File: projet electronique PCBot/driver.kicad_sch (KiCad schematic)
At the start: 1 part, among them U4 DRV8833PWP

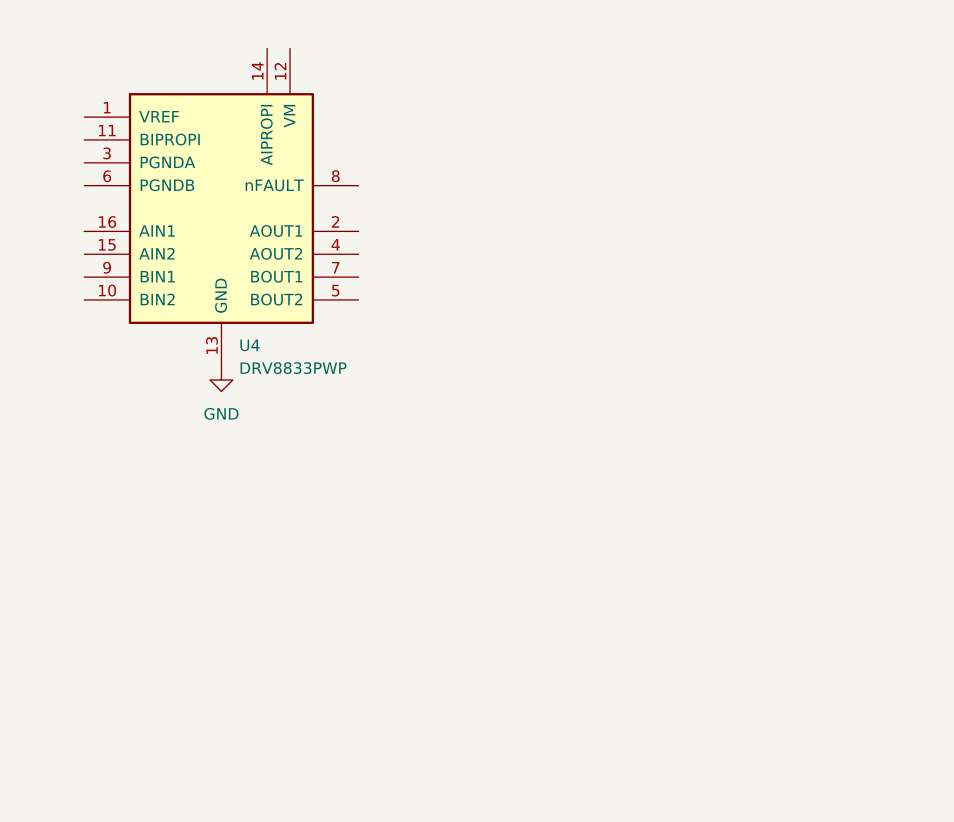
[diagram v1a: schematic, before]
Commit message: feuille driver
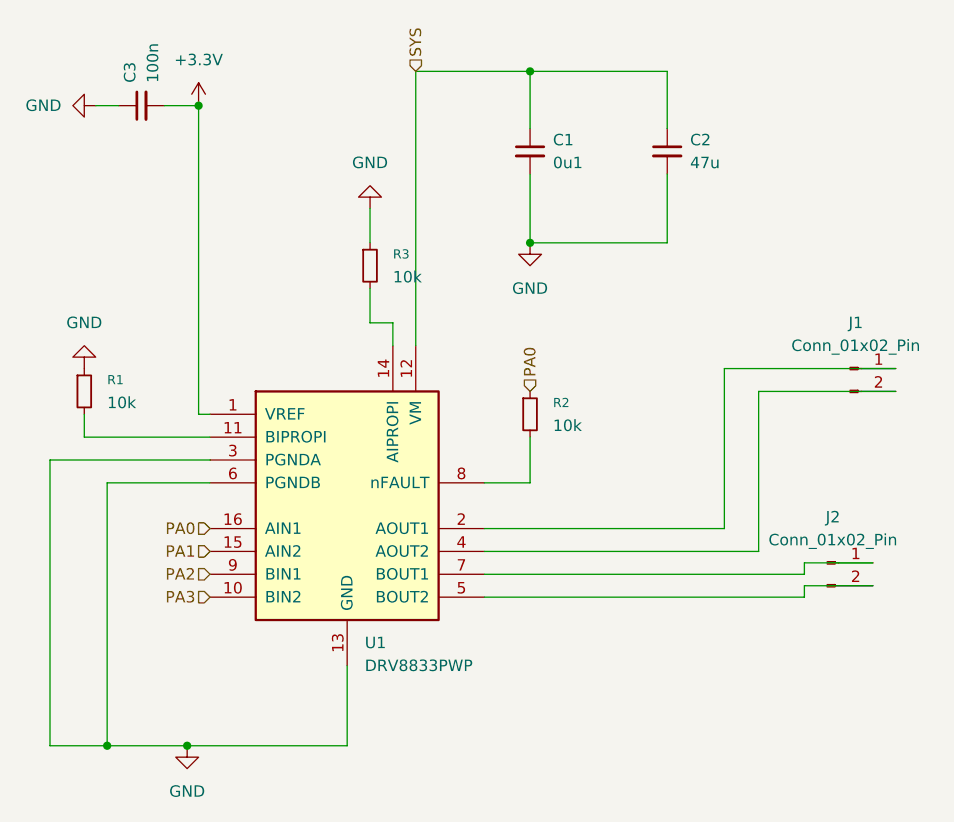
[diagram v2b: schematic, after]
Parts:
- added C1: 0u1, symbol Device:C_Small
- added C2: 47u, symbol Device:C_Small
- added C3: 100n, symbol Device:C_Small
- added J1, J2: Conn_01x02_Pin, symbol Connector:Conn_01x02_Pin
- added R1, R2, R3: 10k, symbol Device:R_Small
- renumbered U4 to U1
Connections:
- net GND: now also U1.3 (PGNDA), U1.6 (PGNDB), C1.2, C2.2, C3.1, R1.1, R3.1
- net +3.3V: now reaches U1.1 (VREF)
- net +3.3V: now also C3.2
- net PA3: now reaches U1.10 (BIN2)
- net at U1.11 (BIPROPI): now also R1.2
- net SYS: now reaches U1.12 (VM)
- net SYS: now also C1.1, C2.1
- net at U1.14 (AIPROPI): now also R3.2
- net PA1: now reaches U1.15 (AIN2)
- net PA0: now reaches U1.16 (AIN1)
- net PA0: now also R2.1
- net at U1.2 (AOUT1): now also J1.1 (Pin_1)
- net at U1.4 (AOUT2): now also J1.2 (Pin_2)
- net at U1.5 (BOUT2): now also J2.2 (Pin_2)
- net at U1.7 (BOUT1): now also J2.1 (Pin_1)
- net at U1.8 (nFAULT): now also R2.2
- net PA2: now reaches U1.9 (BIN1)
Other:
- moved on the sheet: U1

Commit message: feuille driver 2
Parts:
- renumbered C1 to C?, C2 to C?, C3 to C?, J2 to J?, J1 to J?, R1 to R?, R3 to R?, R2 to R?, U1 to U4
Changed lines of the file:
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@@
 		(dnp no)
 		(fields_autoplaced yes)
-		(property "Reference" "J2"
+		(property "Reference" "J?"
 			(at 183.515 118.11 0)
 			(effects
@@
 		)
 		(instances
+			(project "projet electronique PCBot"
+				(path "/210be09d-86cd-4faa-bb91-cc54c5972517/8074907f-d1dc-4b1d-805f-91e9bac82bf7"
+					(reference "J?")
+					(unit 1)
+				)
+			)
 			(project "driver"
 				(path "/7d11412a-f71f-4764-add7-c39197843588"
@@
 		(dnp no)
 		(fields_autoplaced yes)
-		(property "Reference" "#PWR04"
+		(property "Reference" "#PWR?"
 			(at 149.86 93.98 0)
 			(effects
@@
 		)
 		(instances
+			(project "projet electronique PCBot"
+				(path "/210be09d-86cd-4faa-bb91-cc54c5972517/8074907f-d1dc-4b1d-805f-91e9bac82bf7"
+					(reference "#PWR?")
+					(unit 1)
+				)
+			)
 			(project "driver"
 				(path "/7d11412a-f71f-4764-add7-c39197843588"
@@
 		(on_board yes)
 		(dnp no)
-		(property "Reference" "C1"
+		(property "Reference" "C?"
 			(at 152.4 76.2062 0)
 			(effects
@@
 		)
 		(instances
+			(project "projet electronique PCBot"
+				(path "/210be09d-86cd-4faa-bb91-cc54c5972517/8074907f-d1dc-4b1d-805f-91e9bac82bf7"
+					(reference "C?")
+					(unit 1)
+				)
+			)
 			(project ""
 				(path "/7d11412a-f71f-4764-add7-c39197843588"
@@
 		(dnp no)
 		(fields_autoplaced yes)
-		(property "Reference" "#PWR03"
+		(property "Reference" "#PWR?"
 			(at 132.08 77.47 0)
 			(effects
@@
 		)
 		(instances
+			(project "projet electronique PCBot"
+				(path "/210be09d-86cd-4faa-bb91-cc54c5972517/8074907f-d1dc-4b1d-805f-91e9bac82bf7"
+					(reference "#PWR?")
+					(unit 1)
+				)
+			)
 			(project "driver"
 				(path "/7d11412a-f71f-4764-add7-c39197843588"
@@
 		(dnp no)
 		(fields_autoplaced yes)
-		(property "Reference" "J1"
+		(property "Reference" "J?"
 			(at 186.055 96.52 0)
 			(effects
@@
 		)
 		(instances
+			(project "projet electronique PCBot"
+				(path "/210be09d-86cd-4faa-bb91-cc54c5972517/8074907f-d1dc-4b1d-805f-91e9bac82bf7"
+					(reference "J?")
+					(unit 1)
+				)
+			)
 			(project ""
 				(path "/7d11412a-f71f-4764-add7-c39197843588"
@@
 		(dnp no)
 		(fields_autoplaced yes)
-		(property "Reference" "R1"
+		(property "Reference" "R?"
 			(at 102.87 102.8699 0)
 			(effects
@@
 		)
 		(instances
+			(project "projet electronique PCBot"
+				(path "/210be09d-86cd-4faa-bb91-cc54c5972517/8074907f-d1dc-4b1d-805f-91e9bac82bf7"
+					(reference "R?")
+					(unit 1)
+				)
+			)
 			(project ""
 				(path "/7d11412a-f71f-4764-add7-c39197843588"
@@
 		(dnp no)
 		(fields_autoplaced yes)
-		(property "Reference" "C2"
+		(property "Reference" "C?"
 			(at 167.64 76.2062 0)
 			(effects
@@
 		)
 		(instances
+			(project "projet electronique PCBot"
+				(path "/210be09d-86cd-4faa-bb91-cc54c5972517/8074907f-d1dc-4b1d-805f-91e9bac82bf7"
+					(reference "C?")
+					(unit 1)
+				)
+			)
 			(project "driver"
 				(path "/7d11412a-f71f-4764-add7-c39197843588"
@@
 		(on_board yes)
 		(dnp no)
-		(property "Reference" "C3"
+		(property "Reference" "C?"
 			(at 105.4162 69.85 0)
 			(effects
@@
 		)
 		(instances
+			(project "projet electronique PCBot"
+				(path "/210be09d-86cd-4faa-bb91-cc54c5972517/8074907f-d1dc-4b1d-805f-91e9bac82bf7"
+					(reference "C?")
+					(unit 1)
+				)
+			)
 			(project "driver"
 				(path "/7d11412a-f71f-4764-add7-c39197843588"
@@
 		(dnp no)
 		(fields_autoplaced yes)
-		(property "Reference" "#PWR06"
+		(property "Reference" "#PWR?"
 			(at 111.76 149.86 0)
 			(effects
@@
 		)
 		(instances
+			(project "projet electronique PCBot"
+				(path "/210be09d-86cd-4faa-bb91-cc54c5972517/8074907f-d1dc-4b1d-805f-91e9bac82bf7"
+					(reference "#PWR?")
+					(unit 1)
+				)
+			)
 			(project "driver"
 				(path "/7d11412a-f71f-4764-add7-c39197843588"
@@
 		(dnp no)
 		(fields_autoplaced yes)
-		(property "Reference" "#PWR02"
+		(property "Reference" "#PWR?"
 			(at 100.33 95.25 0)
 			(effects
@@
 		)
 		(instances
+			(project "projet electronique PCBot"
+				(path "/210be09d-86cd-4faa-bb91-cc54c5972517/8074907f-d1dc-4b1d-805f-91e9bac82bf7"
+					(reference "#PWR?")
+					(unit 1)
+				)
+			)
 			(project "driver"
 				(path "/7d11412a-f71f-4764-add7-c39197843588"
@@
 		(on_board yes)
 		(dnp no)
-		(property "Reference" "R3"
+		(property "Reference" "R?"
 			(at 134.62 88.8999 0)
 			(effects
@@
 		)
 		(instances
+			(project "projet electronique PCBot"
+				(path "/210be09d-86cd-4faa-bb91-cc54c5972517/8074907f-d1dc-4b1d-805f-91e9bac82bf7"
+					(reference "R?")
+					(unit 1)
+				)
+			)
 			(project ""
 				(path "/7d11412a-f71f-4764-add7-c39197843588"
@@
 		(on_board yes)
 		(dnp no)
-		(property "Reference" "U1"
+		(property "Reference" "U4"
 			(at 131.4959 132.08 0)
 			(effects
@@
 		(dnp no)
 		(fields_autoplaced yes)
-		(property "Reference" "R2"
+		(property "Reference" "R?"
 			(at 152.4 105.4099 0)
 			(effects
@@
 		)
 		(instances
+			(project "projet electronique PCBot"
+				(path "/210be09d-86cd-4faa-bb91-cc54c5972517/8074907f-d1dc-4b1d-805f-91e9bac82bf7"
+					(reference "R?")
+					(unit 1)
+				)
+			)
 			(project ""
 				(path "/7d11412a-f71f-4764-add7-c39197843588"
@@
 		(dnp no)
 		(fields_autoplaced yes)
-		(property "Reference" "#PWR01"
+		(property "Reference" "#PWR?"
 			(at 95.25 72.39 0)
 			(effects
@@
 		)
 		(instances
+			(project "projet electronique PCBot"
+				(path "/210be09d-86cd-4faa-bb91-cc54c5972517/8074907f-d1dc-4b1d-805f-91e9bac82bf7"
+					(reference "#PWR?")
+					(unit 1)
+				)
+			)
 			(project ""
 				(path "/7d11412a-f71f-4764-add7-c39197843588"
@@
 		(dnp no)
 		(fields_autoplaced yes)
-		(property "Reference" "#PWR05"
+		(property "Reference" "#PWR?"
 			(at 113.03 76.2 0)
 			(effects
@@
 		)
 		(instances
+			(project "projet electronique PCBot"
+				(path "/210be09d-86cd-4faa-bb91-cc54c5972517/8074907f-d1dc-4b1d-805f-91e9bac82bf7"
+					(reference "#PWR?")
+					(unit 1)
+				)
+			)
 			(project ""
 				(path "/7d11412a-f71f-4764-add7-c39197843588"

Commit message: fichier driver et gestion d'energie
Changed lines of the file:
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@@
+	(wire
+		(pts
+			(xy 149.86 99.06) (xy 149.86 104.14)
+		)
+		(stroke
+			(width 0)
+			(type default)
+		)
+	)
 	(wire
 		(pts
@@
 	(hierarchical_label "PA0"
 		(shape input)
-		(at 149.86 104.14 90)
+		(at 149.86 99.06 90)
 		(effects
 			(font

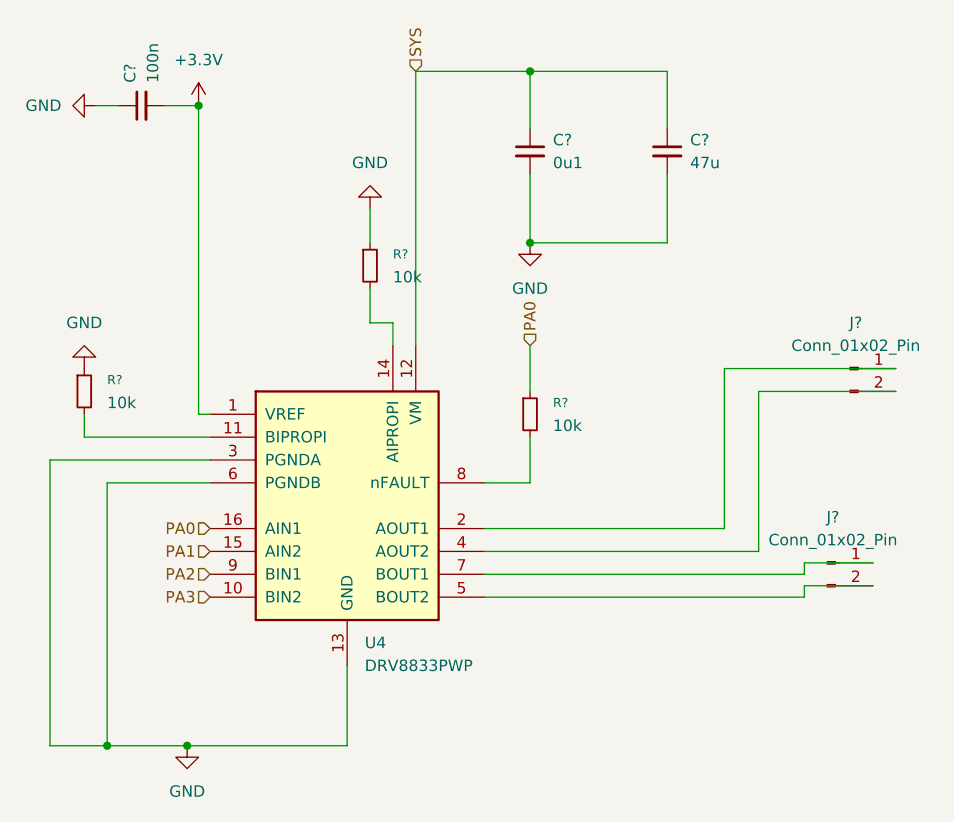
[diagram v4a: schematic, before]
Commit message: ajout de connexions
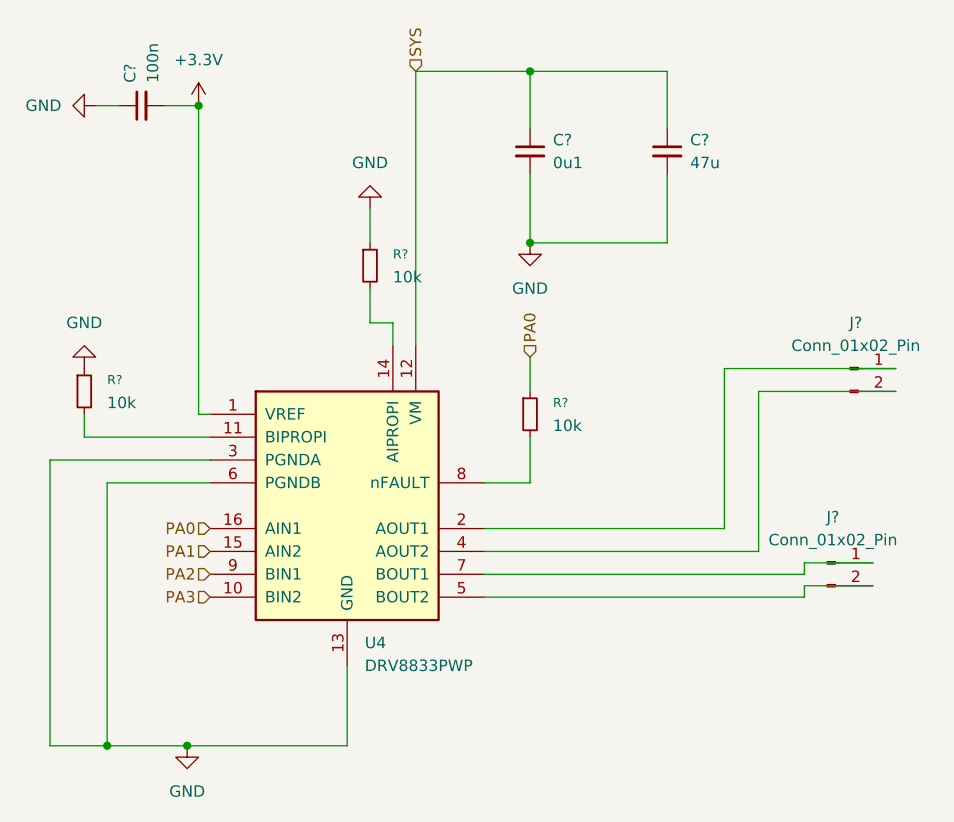
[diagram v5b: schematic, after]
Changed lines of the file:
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@@
 	(wire
 		(pts
-			(xy 149.86 99.06) (xy 149.86 104.14)
+			(xy 149.86 100.33) (xy 149.86 104.14)
 		)
 		(stroke
@@
 	(hierarchical_label "PA0"
 		(shape input)
-		(at 149.86 99.06 90)
+		(at 149.86 100.33 90)
 		(effects
 			(font
